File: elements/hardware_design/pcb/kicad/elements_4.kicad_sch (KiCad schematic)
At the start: 73 parts

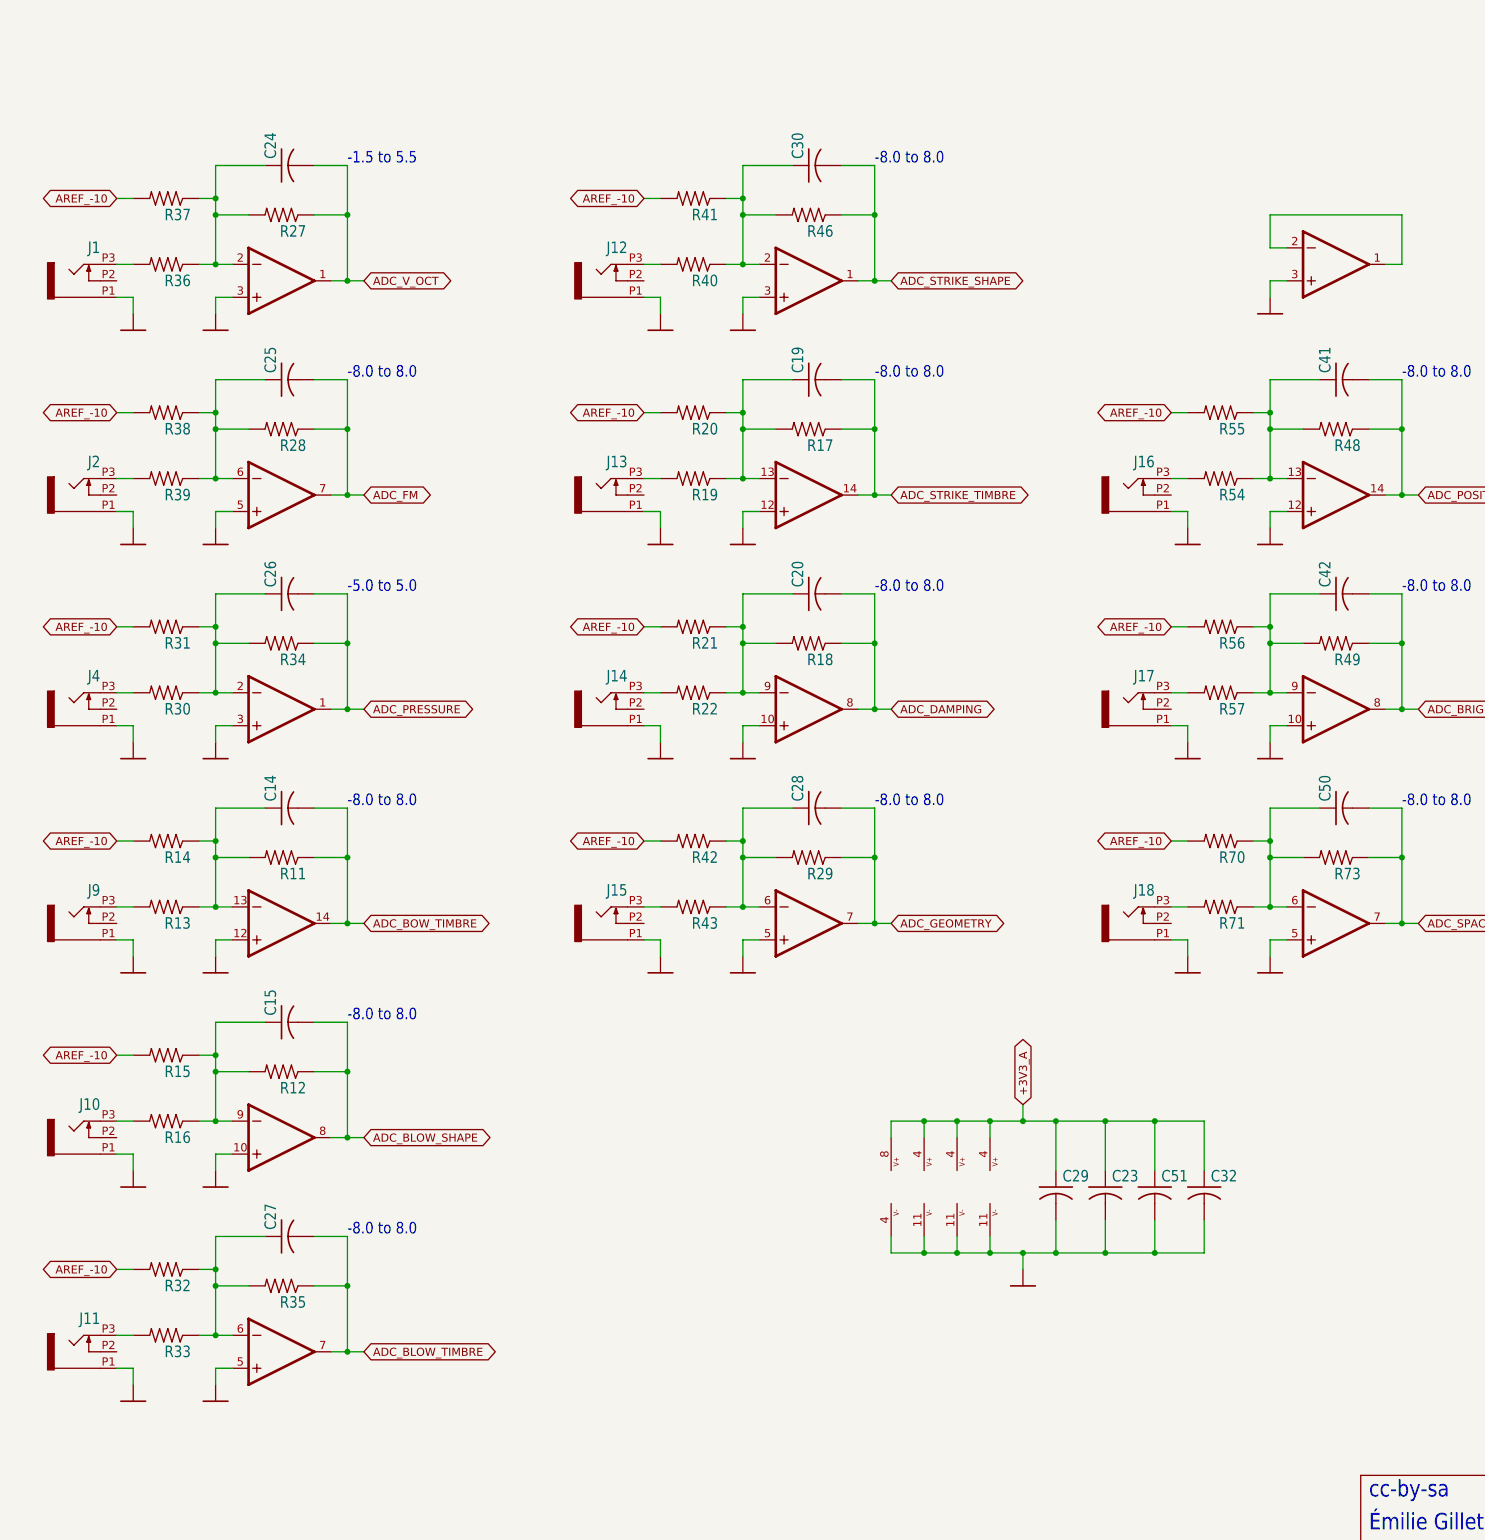
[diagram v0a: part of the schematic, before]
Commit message: swap wm8731 package (haven't drawn traces yet)
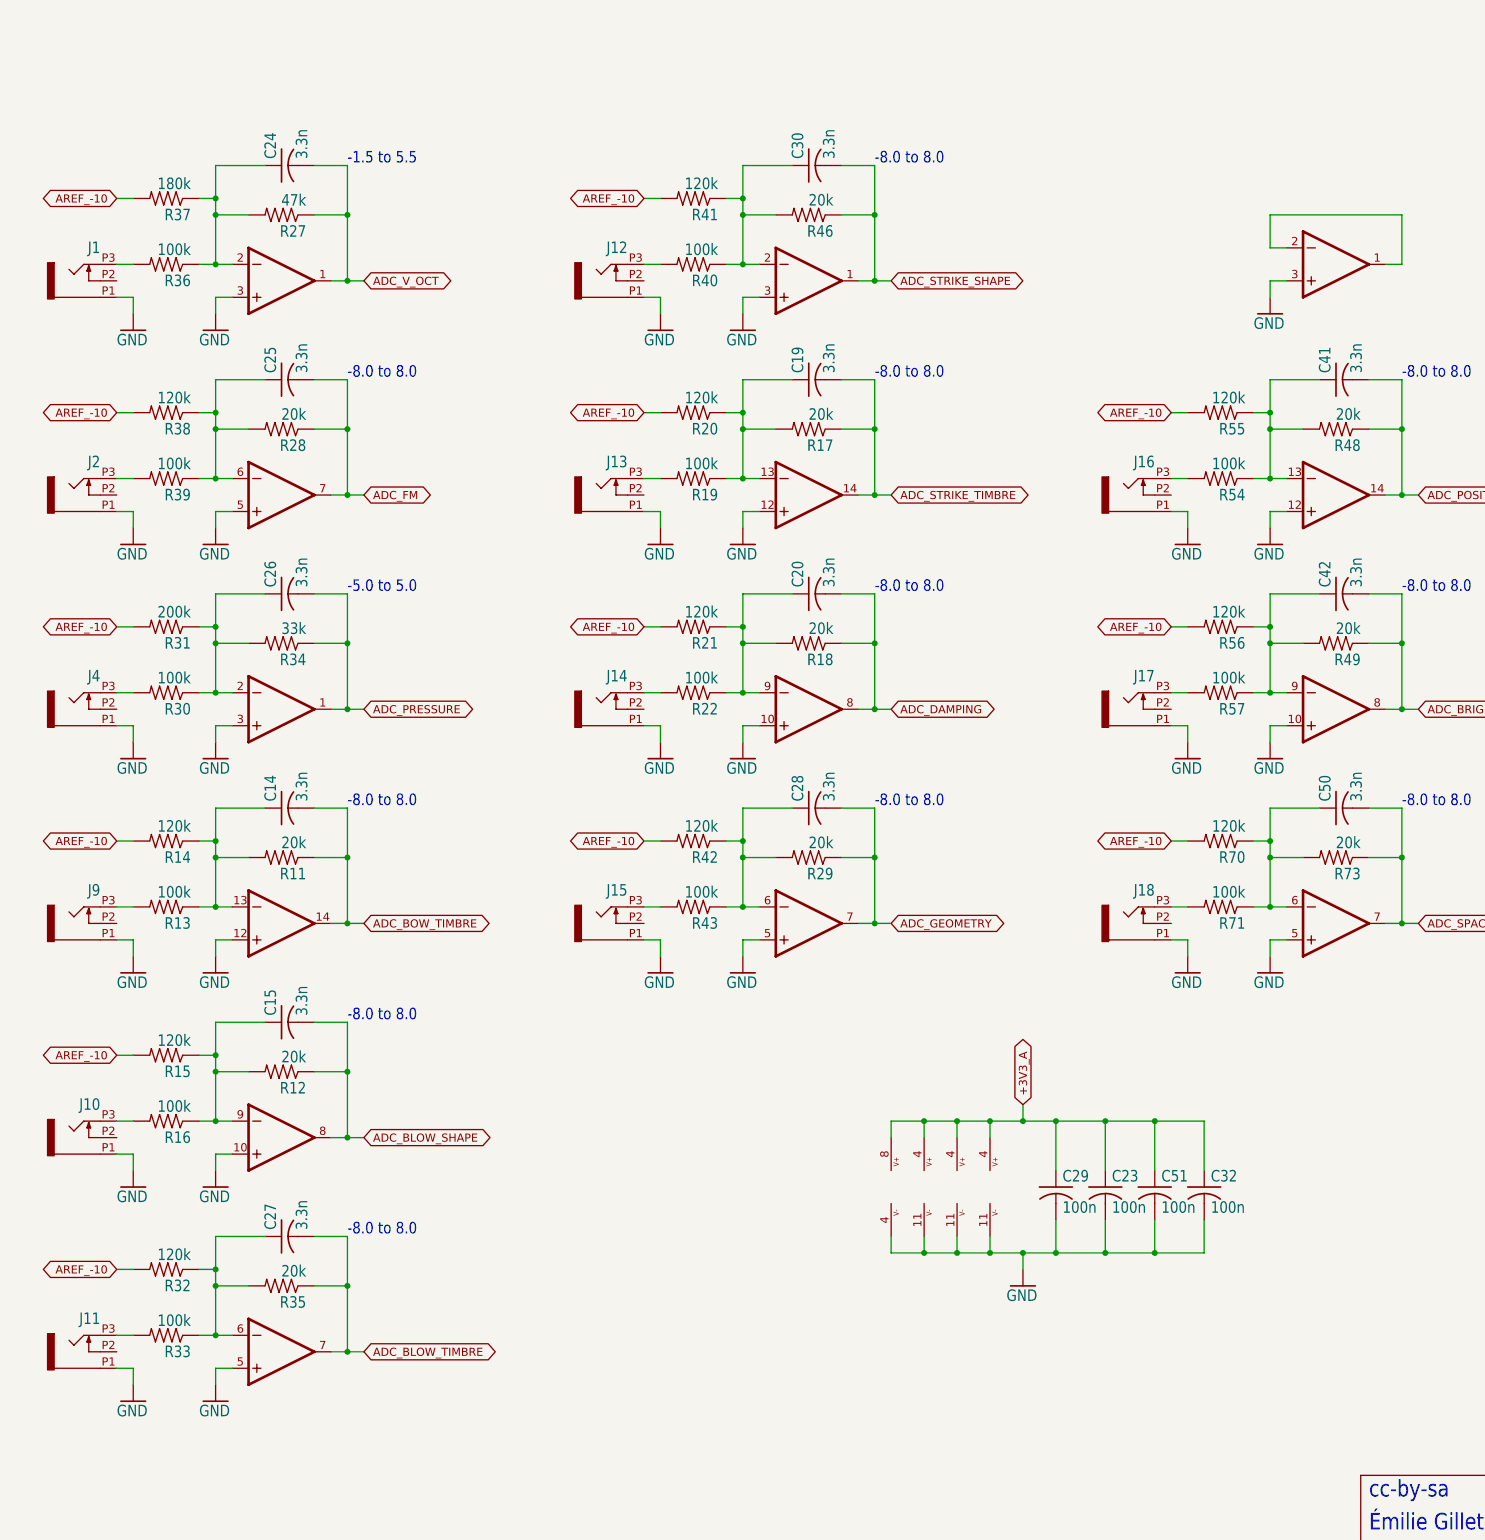
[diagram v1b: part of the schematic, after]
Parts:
- C14, C15, C19, C20, C24, C25, C26, C27, C28, C30, C41, C42, C50: value (none) -> 3.3n; footprint (none) -> elements:C0603
- C23, C29, C32, C51: value (none) -> 100n; footprint (none) -> elements:C0603
- IC13, IC6, IC7: value (none) -> MCP6004; footprint (none) -> elements:SO14
- IC9: value (none) -> MCP6002; footprint (none) -> elements:SO08
- J1, J10, J11, J12, J13, J14, J15, J16, J17, J18, J2, J4, J9: value (none) -> PJ301_THONKICONN6; footprint (none) -> elements:WQP_PJ_301M6
- R11, R12, R17, R18, R28, R29, R35, R46, R48, R49, R73: value (none) -> 20k; footprint (none) -> elements:R0603
- R13, R16, R19, R22, R30, R33, R36, R39, R40, R43, R54, R57, R71: value (none) -> 100k; footprint (none) -> elements:R0603
- R14, R15, R20, R21, R32, R38, R41, R42, R55, R56, R70: value (none) -> 120k; footprint (none) -> elements:R0603
- R27: value (none) -> 47k; footprint (none) -> elements:R0603
- R31: value (none) -> 200k; footprint (none) -> elements:R0603
- R34: value (none) -> 33k; footprint (none) -> elements:R0603
- R37: value (none) -> 180k; footprint (none) -> elements:R0603
